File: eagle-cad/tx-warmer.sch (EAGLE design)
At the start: 22 parts, among them IC2 MCP1702

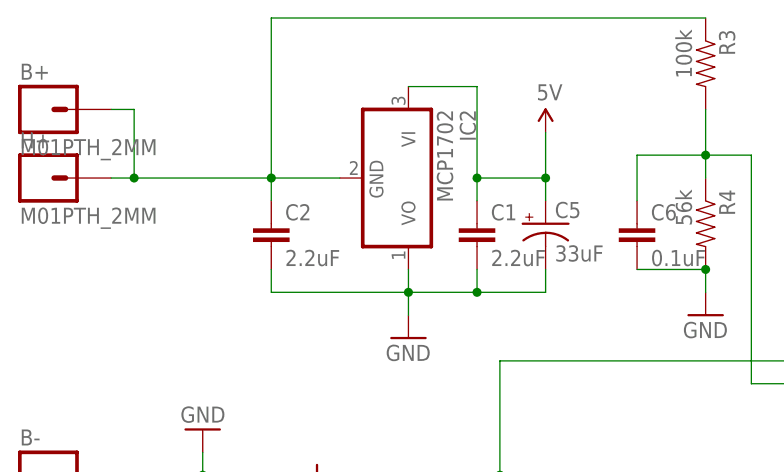
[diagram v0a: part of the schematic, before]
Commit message: Changed voltage regulator MCP1702 to LP2950 (formed leads)
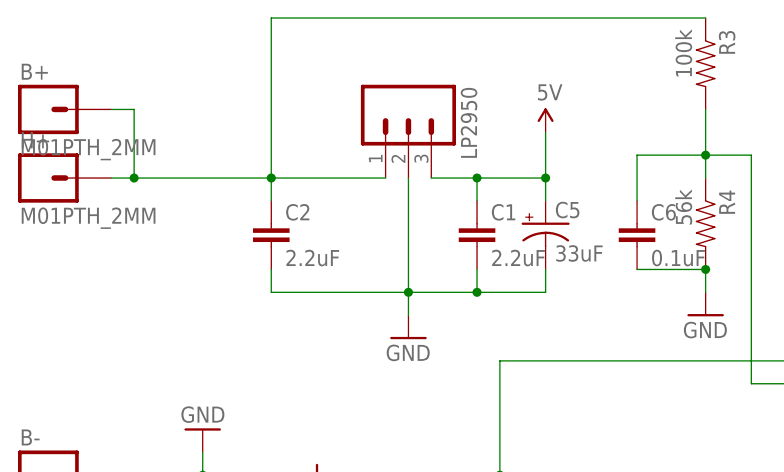
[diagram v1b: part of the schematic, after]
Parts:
- removed IC2: MCP1702, linear:78L05Z
- added LP2950: (no value), SparkFun-Connectors:M031X03_NO_SILK
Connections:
- net 5V: now also LP2950.3; no longer IC2.VI
- net GND: now also LP2950.2; no longer IC2.VO
- net N$4: now also LP2950.1; no longer IC2.GND
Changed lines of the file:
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@@
 <part name="ATTINY84A" library="ic-package" deviceset="DIL14" device="S"/>
 <part name="IRLB8743" library="transistor-fet" deviceset="IRF510" device="" value="IRLB8743"/>
-<part name="IC2" library="linear" deviceset="78*" device="Z" technology="L05" value="MCP1702"/>
 <part name="GND1" library="SparkFun-Aesthetics" deviceset="GND" device=""/>
 <part name="U$1" library="SparkFun-Aesthetics" deviceset="5V" device=""/>
@@
 <part name="B-" library="SparkFun-Connectors" deviceset="M01" device="PTH_2MM"/>
 <part name="H-" library="SparkFun-Connectors" deviceset="M01" device="PTH_2MM"/>
+<part name="LP2950" library="SparkFun-Connectors" deviceset="M03" device="1X03_NO_SILK"/>
 </parts>
 <sheets>
@@
 <instance part="ATTINY84A" gate="G$1" x="111.76" y="53.34"/>
 <instance part="IRLB8743" gate="G$1" x="25.4" y="35.56" rot="R180"/>
-<instance part="IC2" gate="A1" x="35.56" y="71.12" rot="R270"/>
 <instance part="GND1" gate="1" x="35.56" y="53.34"/>
 <instance part="U$1" gate="G$1" x="50.8" y="76.2"/>
@@
 <instance part="B-" gate="G$1" x="-5.08" y="38.1"/>
 <instance part="H-" gate="G$1" x="-5.08" y="33.02"/>
+<instance part="LP2950" gate="G$1" x="35.56" y="78.74" rot="R270"/>
 </instances>
 <busses>
@@
 <wire x1="20.32" y1="88.9" x2="68.58" y2="88.9" width="0.1524" layer="91"/>
 <pinref part="R3" gate="G$1" pin="1"/>
-<pinref part="IC2" gate="A1" pin="GND"/>
-<wire x1="20.32" y1="71.12" x2="27.94" y2="71.12" width="0.1524" layer="91"/>
+<wire x1="20.32" y1="71.12" x2="33.02" y2="71.12" width="0.1524" layer="91"/>
 <pinref part="C2" gate="G$1" pin="1"/>
 <pinref part="B+" gate="G$1" pin="1"/>
 <pinref part="H+" gate="G$1" pin="1"/>
+<pinref part="LP2950" gate="G$1" pin="1"/>
 </segment>
 </net>
@@
 <wire x1="35.56" y1="58.42" x2="35.56" y2="55.88" width="0.1524" layer="91"/>
 <junction x="35.56" y="58.42"/>
-<pinref part="IC2" gate="A1" pin="VO"/>
-<wire x1="35.56" y1="58.42" x2="35.56" y2="60.96" width="0.1524" layer="91"/>
 <wire x1="43.18" y1="58.42" x2="50.8" y2="58.42" width="0.1524" layer="91"/>
 <wire x1="50.8" y1="58.42" x2="50.8" y2="60.96" width="0.1524" layer="91"/>
@@
 <pinref part="C1" gate="G$1" pin="2"/>
 <pinref part="C2" gate="G$1" pin="2"/>
+<pinref part="LP2950" gate="G$1" pin="2"/>
+<wire x1="35.56" y1="58.42" x2="35.56" y2="71.12" width="0.1524" layer="91"/>
 </segment>
 <segment>
@@
 <segment>
 <wire x1="43.18" y1="68.58" x2="43.18" y2="71.12" width="0.1524" layer="91"/>
-<pinref part="IC2" gate="A1" pin="VI"/>
-<wire x1="35.56" y1="81.28" x2="43.18" y2="81.28" width="0.1524" layer="91"/>
-<wire x1="43.18" y1="81.28" x2="43.18" y2="71.12" width="0.1524" layer="91"/>
-<junction x="43.18" y="71.12"/>
 <wire x1="43.18" y1="71.12" x2="50.8" y2="71.12" width="0.1524" layer="91"/>
 <wire x1="50.8" y1="71.12" x2="50.8" y2="68.58" width="0.1524" layer="91"/>
@@
 <junction x="50.8" y="71.12"/>
 <pinref part="C1" gate="G$1" pin="1"/>
+<pinref part="LP2950" gate="G$1" pin="3"/>
+<wire x1="43.18" y1="71.12" x2="38.1" y2="71.12" width="0.1524" layer="91"/>
+<junction x="43.18" y="71.12"/>
 </segment>
 </net>

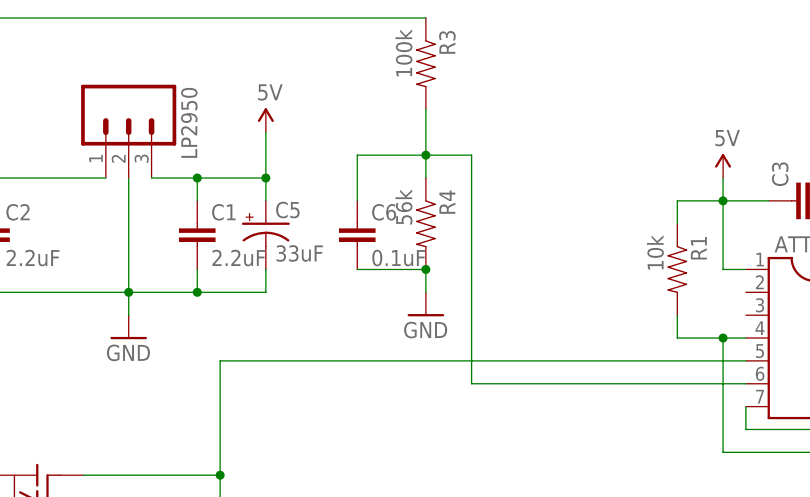
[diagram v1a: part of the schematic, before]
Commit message: Modified voltage divider to support higher voltages (max now 20.1V)
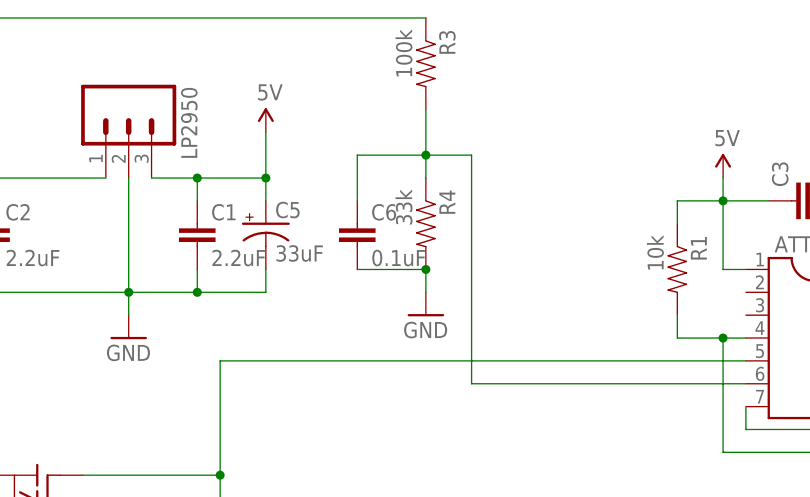
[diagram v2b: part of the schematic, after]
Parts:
- R4: value 56k -> 33k
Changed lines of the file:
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@@
 <part name="R6" library="SparkFun-Resistors" deviceset="RESISTOR" device="EZ" value="100k"/>
 <part name="R3" library="SparkFun-Resistors" deviceset="RESISTOR" device="EZ" value="100k"/>
-<part name="R4" library="SparkFun-Resistors" deviceset="RESISTOR" device="EZ" value="56k"/>
+<part name="R4" library="SparkFun-Resistors" deviceset="RESISTOR" device="EZ" value="33k"/>
 <part name="GND6" library="SparkFun-Aesthetics" deviceset="GND" device=""/>
 <part name="LED1" library="SparkFun-LED" deviceset="LED" device="5MM-KIT" value="GREEN"/>

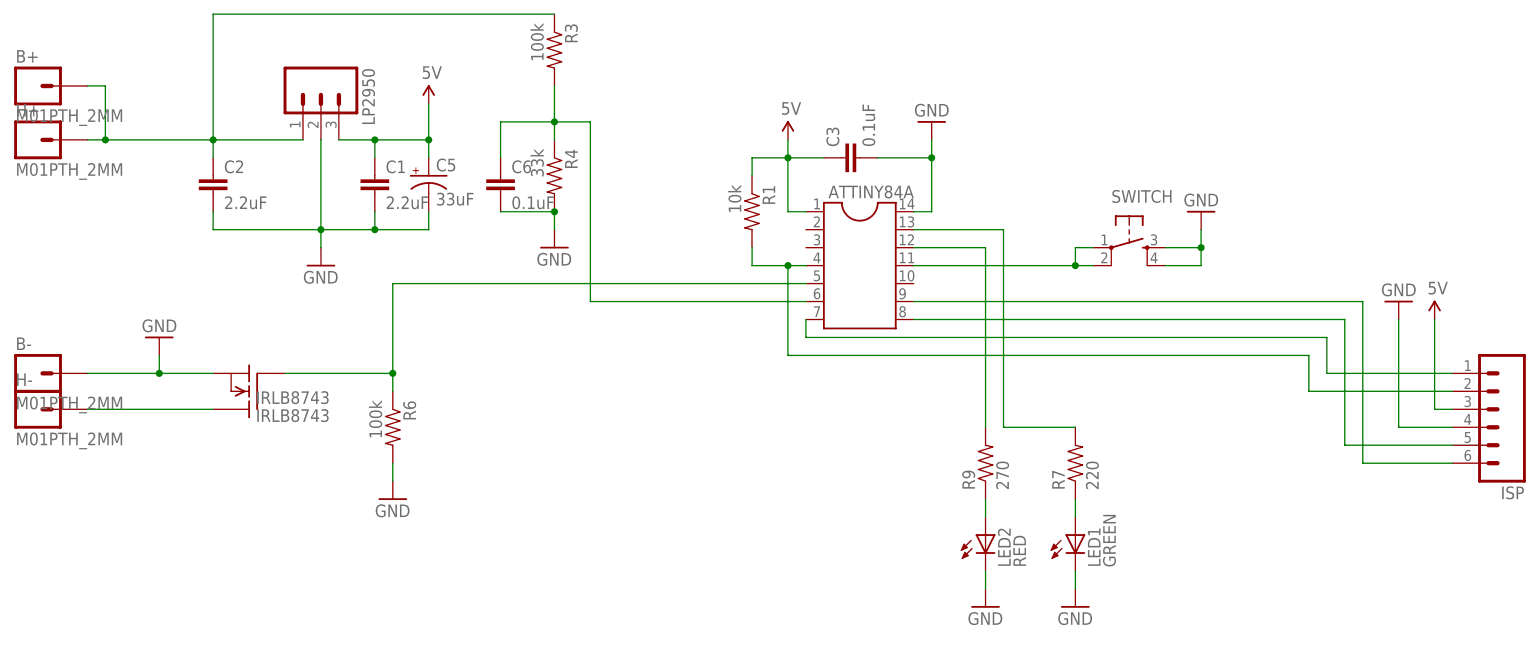
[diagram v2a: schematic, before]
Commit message: Removed ISP-header. Mainly useless and made room for future changes
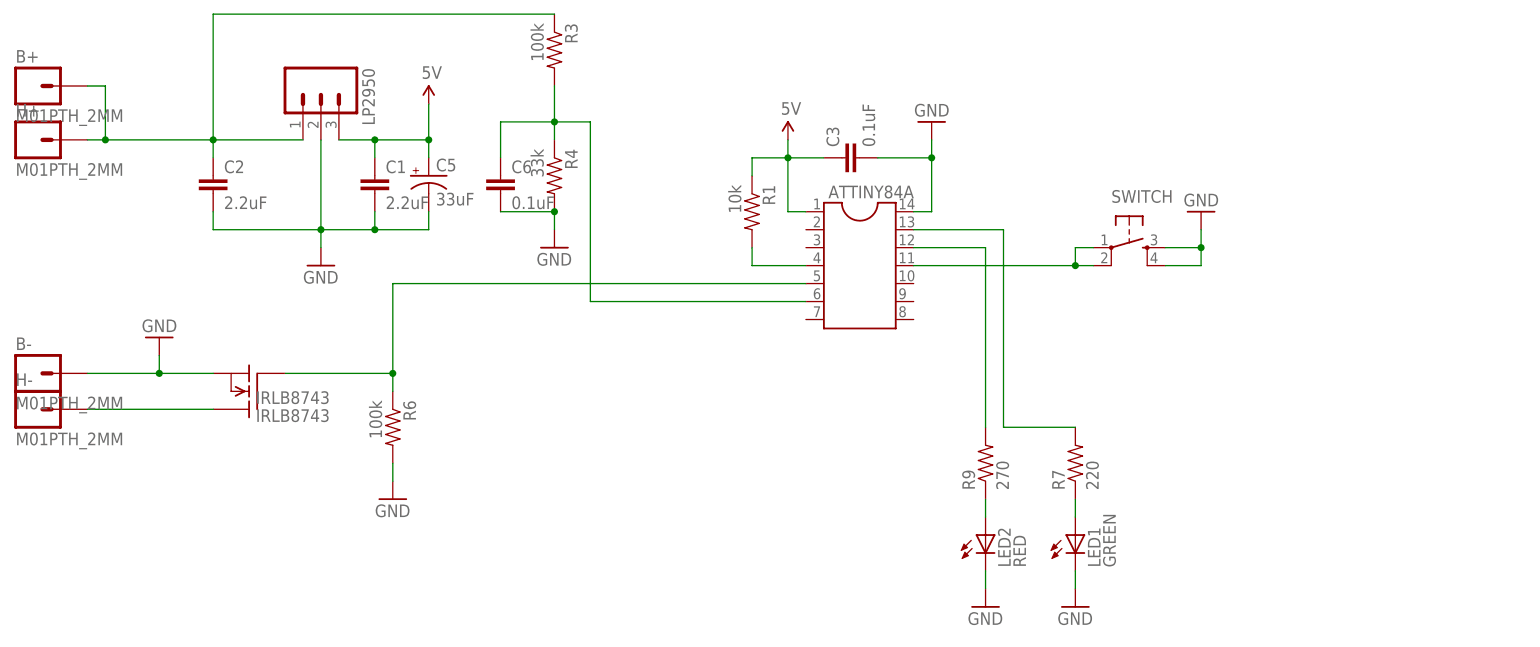
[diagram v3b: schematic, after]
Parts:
- removed ISP: (no value), SparkFun-Connectors:M06LOCK_LONGPADS
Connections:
- removed net N$2: ATTINY84A.8, ISP.5
- removed net N$3: ATTINY84A.7, ISP.1
- removed net N$5: ATTINY84A.9, ISP.6
- net 5V: no longer ISP.3
- net GND: no longer ISP.4
- net N$11: no longer ISP.2
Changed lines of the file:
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@@
 <part name="LED1" library="SparkFun-LED" deviceset="LED" device="5MM-KIT" value="GREEN"/>
 <part name="LED2" library="SparkFun-LED" deviceset="LED" device="5MM-KIT" value="RED"/>
-<part name="U$4" library="SparkFun-Aesthetics" deviceset="5V" device=""/>
-<part name="GND4" library="SparkFun-Aesthetics" deviceset="GND" device=""/>
-<part name="ISP" library="SparkFun-Connectors" deviceset="M06" device="LOCK_LONGPADS"/>
 <part name="C5" library="SparkFun-Capacitors" deviceset="CAP_POL" device="PTH2" value="33uF"/>
 <part name="C6" library="SparkFun-Passives" deviceset="CAP" device="EZ" value="0.1uF"/>
@@
 <instance part="LED1" gate="G$1" x="142.24" y="15.24"/>
 <instance part="LED2" gate="G$1" x="129.54" y="15.24"/>
-<instance part="U$4" gate="G$1" x="193.04" y="45.72"/>
-<instance part="GND4" gate="1" x="187.96" y="48.26" rot="R180"/>
-<instance part="ISP" gate="G$1" x="200.66" y="33.02" rot="R180"/>
 <instance part="C5" gate="G$1" x="50.8" y="66.04"/>
 <instance part="C6" gate="G$1" x="60.96" y="63.5"/>
@@
 <pinref part="GND6" gate="1" pin="GND"/>
 </segment>
-<segment>
-<pinref part="GND4" gate="1" pin="GND"/>
-<wire x1="187.96" y1="45.72" x2="187.96" y2="30.48" width="0.1524" layer="91"/>
-<pinref part="ISP" gate="G$1" pin="4"/>
-<wire x1="187.96" y1="30.48" x2="195.58" y2="30.48" width="0.1524" layer="91"/>
-</segment>
 </net>
 <net name="5V" class="0">
@@
 <wire x1="96.52" y1="66.04" x2="96.52" y2="68.58" width="0.1524" layer="91"/>
 <wire x1="96.52" y1="68.58" x2="101.6" y2="68.58" width="0.1524" layer="91"/>
-</segment>
-<segment>
-<pinref part="U$4" gate="G$1" pin="5V"/>
-<wire x1="193.04" y1="45.72" x2="193.04" y2="33.02" width="0.1524" layer="91"/>
-<pinref part="ISP" gate="G$1" pin="3"/>
-<wire x1="193.04" y1="33.02" x2="195.58" y2="33.02" width="0.1524" layer="91"/>
 </segment>
 <segment>
@@
 </segment>
 </net>
-<net name="N$2" class="0">
-<segment>
-<pinref part="ATTINY84A" gate="G$1" pin="8"/>
-<wire x1="119.38" y1="45.72" x2="180.34" y2="45.72" width="0.1524" layer="91"/>
-<pinref part="ISP" gate="G$1" pin="5"/>
-<wire x1="195.58" y1="27.94" x2="180.34" y2="27.94" width="0.1524" layer="91"/>
-<wire x1="180.34" y1="45.72" x2="180.34" y2="27.94" width="0.1524" layer="91"/>
-</segment>
-</net>
-<net name="N$3" class="0">
-<segment>
-<pinref part="ATTINY84A" gate="G$1" pin="7"/>
-<wire x1="104.14" y1="45.72" x2="104.14" y2="43.18" width="0.1524" layer="91"/>
-<wire x1="104.14" y1="43.18" x2="177.8" y2="43.18" width="0.1524" layer="91"/>
-<wire x1="177.8" y1="43.18" x2="177.8" y2="38.1" width="0.1524" layer="91"/>
-<pinref part="ISP" gate="G$1" pin="1"/>
-<wire x1="177.8" y1="38.1" x2="195.58" y2="38.1" width="0.1524" layer="91"/>
-</segment>
-</net>
-<net name="N$5" class="0">
-<segment>
-<pinref part="ATTINY84A" gate="G$1" pin="9"/>
-<wire x1="119.38" y1="48.26" x2="182.88" y2="48.26" width="0.1524" layer="91"/>
-<wire x1="182.88" y1="48.26" x2="182.88" y2="25.4" width="0.1524" layer="91"/>
-<pinref part="ISP" gate="G$1" pin="6"/>
-<wire x1="182.88" y1="25.4" x2="195.58" y2="25.4" width="0.1524" layer="91"/>
-</segment>
-</net>
 <net name="N$11" class="0">
 <segment>
 <pinref part="ATTINY84A" gate="G$1" pin="4"/>
-<wire x1="104.14" y1="53.34" x2="101.6" y2="53.34" width="0.1524" layer="91"/>
-<wire x1="101.6" y1="53.34" x2="101.6" y2="40.64" width="0.1524" layer="91"/>
-<wire x1="101.6" y1="40.64" x2="175.26" y2="40.64" width="0.1524" layer="91"/>
-<wire x1="175.26" y1="40.64" x2="175.26" y2="35.56" width="0.1524" layer="91"/>
-<pinref part="ISP" gate="G$1" pin="2"/>
-<wire x1="175.26" y1="35.56" x2="195.58" y2="35.56" width="0.1524" layer="91"/>
 <pinref part="R1" gate="G$1" pin="2"/>
-<wire x1="101.6" y1="53.34" x2="96.52" y2="53.34" width="0.1524" layer="91"/>
+<wire x1="104.14" y1="53.34" x2="96.52" y2="53.34" width="0.1524" layer="91"/>
 <wire x1="96.52" y1="53.34" x2="96.52" y2="55.88" width="0.1524" layer="91"/>
-<junction x="101.6" y="53.34"/>
-</segment>
-</net>
+</segment>
+</net>

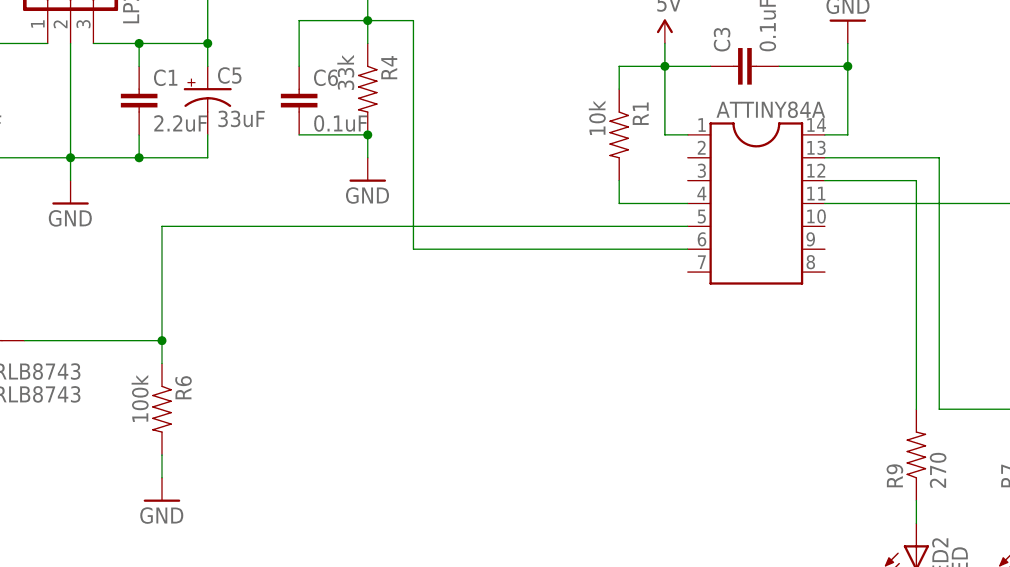
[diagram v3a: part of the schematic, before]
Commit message: Moved PWM from pin5 to pin8
Reason for this to utilizer timer1 and allows using prescaler without
interference to delay-methods.
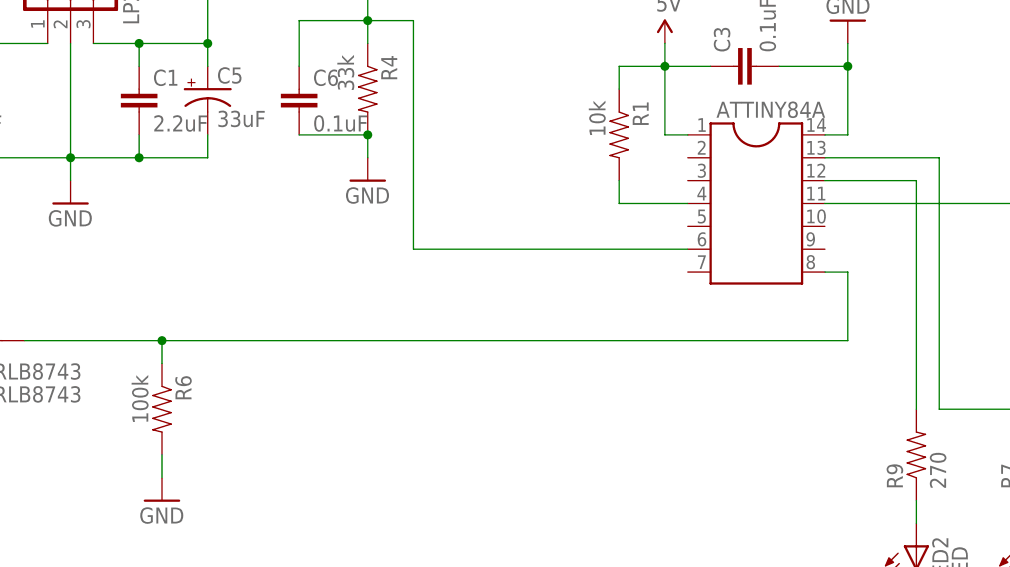
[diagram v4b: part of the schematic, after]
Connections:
- net N$6: now also ATTINY84A.8; no longer ATTINY84A.5
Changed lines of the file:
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@@
 <wire x1="45.72" y1="38.1" x2="30.48" y2="38.1" width="0.1524" layer="91"/>
 <wire x1="45.72" y1="35.56" x2="45.72" y2="38.1" width="0.1524" layer="91"/>
-<pinref part="ATTINY84A" gate="G$1" pin="5"/>
-<wire x1="104.14" y1="50.8" x2="45.72" y2="50.8" width="0.1524" layer="91"/>
-<wire x1="45.72" y1="50.8" x2="45.72" y2="38.1" width="0.1524" layer="91"/>
+<pinref part="R6" gate="G$1" pin="1"/>
+<wire x1="45.72" y1="38.1" x2="121.92" y2="38.1" width="0.1524" layer="91"/>
+<wire x1="121.92" y1="38.1" x2="121.92" y2="45.72" width="0.1524" layer="91"/>
+<pinref part="ATTINY84A" gate="G$1" pin="8"/>
+<wire x1="121.92" y1="45.72" x2="119.38" y2="45.72" width="0.1524" layer="91"/>
 <junction x="45.72" y="38.1"/>
-<pinref part="R6" gate="G$1" pin="1"/>
 </segment>
 </net>
